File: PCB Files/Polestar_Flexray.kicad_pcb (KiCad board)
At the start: 4 copper layers, 82 x 43 mm, 80 parts, among them J1 JAE DX07S024XJ1R1100, J2 Molex 2125280400, J3 JAE MX34032NF4, J4 JAE MX34032NF4, K1 G5V-2-H1 DC12, K2 G5V-2-H1 DC12, K3 G5V-2-H1 DC12, Q1 DMN3200U-7, Q2 DMN3200U-7, Q3 DMP4015SSS-13, U1 Vishay DG419LEDY-T1-GE4, U2 Vishay DG419LEDY-T1-GE4, U3 LM53600LQDSXRQ1, U4 XIAO_RP2350, U5 TJA1082, U6 TJA1082, U8 TCAN4550-Q1, Y1 40MHz NX2016SA

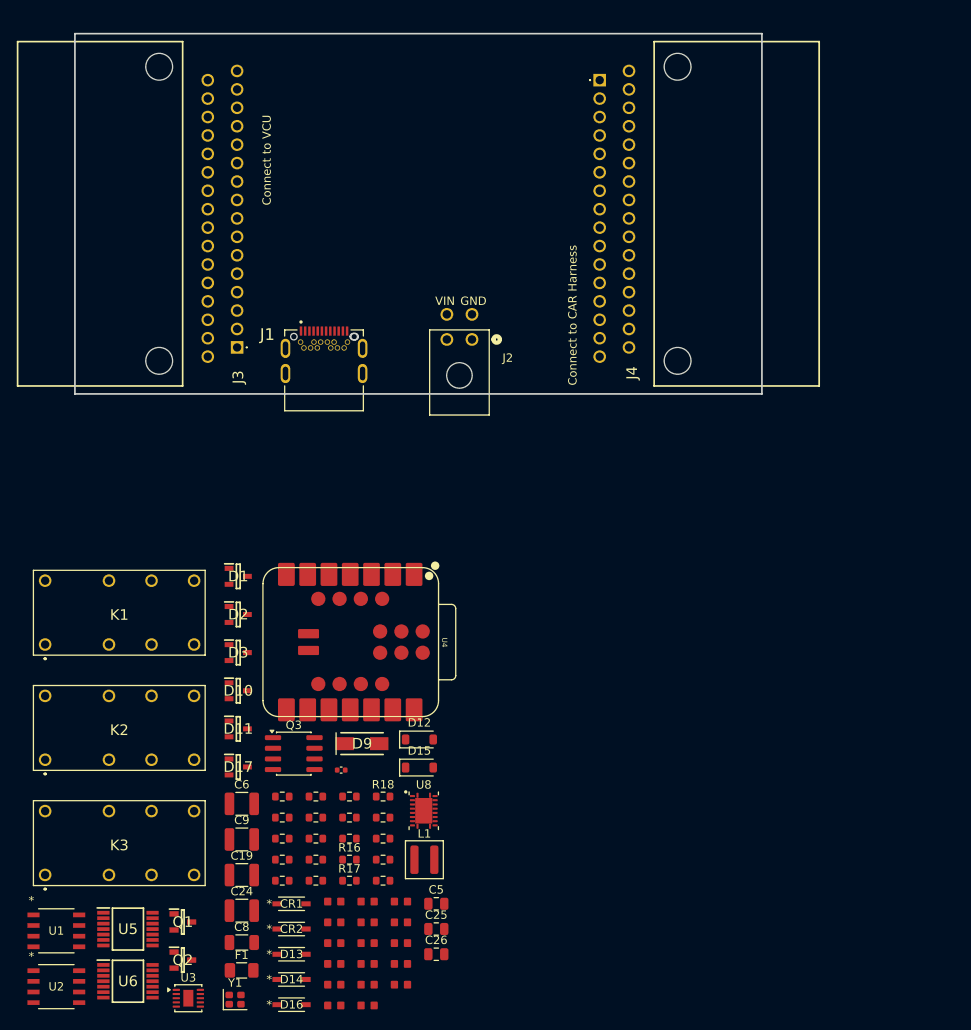
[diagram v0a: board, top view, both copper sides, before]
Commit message: Re-place board on 98x58 mm outline, add mounting holes and rounded corners
Placement
- Re-placed all 80 footprints to the "wide_2" layout on a 98 x 58 mm
  outline (was 119 x 43 mm). The 5 V buck block (U3, L1, C8-C12, C27,
  R13) and D9/C6 move to the bottom right, the SW_VCC group (D15, R21,
  D16) to the top left, and the comma CAN group (U1, U2, R2, R3, C28)
  shifts left. C11, D9, R13 and R21 also change rotation.
- Pad geometry, sizes, layers and nets verified unchanged across the
  rotations: 389 pads, 126 nets, 0 net changes.

Mechanical
- Added H1-H4: M3, 3.2 mm, non-plated, inset 3.8 mm from both edges.
  Non-plated so enclosure screws do not bond chassis to board ground;
  harness pin 13 is not board GND. PCB-only, no schematic symbols.
- Radiused the four board corners at R3.8 mm. Each arc centre lands on
  its mounting-hole centre, so the corner is concentric with the hole.
- Reshaped the In1.Cu ground pour outline to match the rounded corners
  and dropped its stale square-cornered fill so it repours correctly.

DRC
- Added Polestar_Flexray.kicad_dru. U8 reproduces TI drawing 4225320/A
  (RGY0020A) exactly, which places the exposed pad 0.025 mm from every
  perimeter pin; U3's 0.5 mm-pitch pins sit 0.26 mm apart against a
  0.3 mm Power netclass rule. Both are non-solder-mask-defined, so
  bridging is controlled by the stencil, not copper spacing. The rule
  is scoped to U3/U8 so other footprints are still checked normally.
- Raised U4's reference text from 0.635 mm to 1.0 mm to meet the
  0.8 mm board minimum.
- Now 0 clearance, 0 courtyard-overlap, 0 copper-to-edge and
  0 invalid-outline violations. Remaining items are the 239 unrouted
  ratsnest connections and cosmetic silkscreen warnings.

The board is still unrouted - 0 tracks, 0 vias. Do not fabricate.

Co-Authored-By: Claude Opus 5 <noreply@anthropic.com>
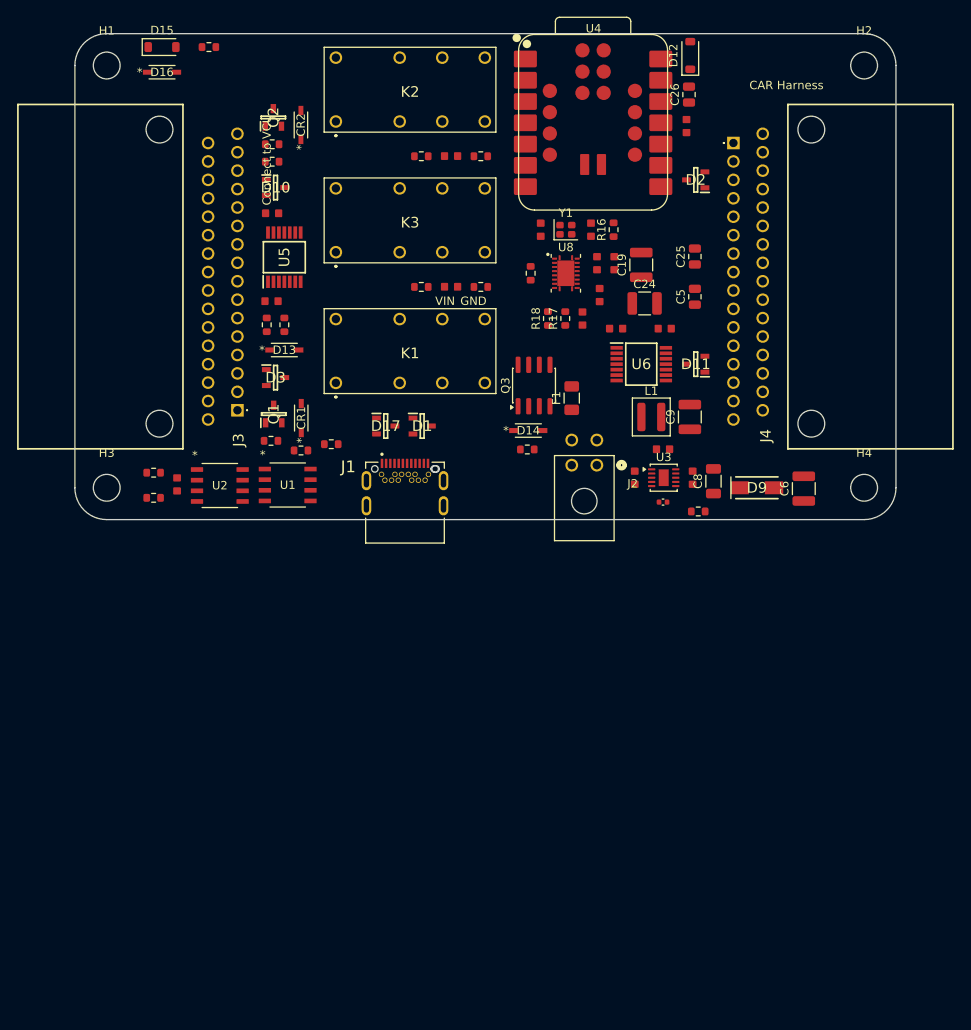
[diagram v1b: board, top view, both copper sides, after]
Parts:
- added H1: MountingHole_3.2mm_M3, MountingHole_3.2mm_M3, F.Cu at (105.8, 73.3)
- added H2: MountingHole_3.2mm_M3, MountingHole_3.2mm_M3, F.Cu at (196.2, 73.3)
- added H3: MountingHole_3.2mm_M3, MountingHole_3.2mm_M3, F.Cu at (105.8, 123.7)
- added H4: MountingHole_3.2mm_M3, MountingHole_3.2mm_M3, F.Cu at (196.2, 123.7)
- moved D16 112.4 mm to (112.4, 74.1)
- moved C7 110.8 mm to (175.0, 80.5), turned to 90 degrees
- moved C26 106.9 mm to (175.3, 76.8), turned to 90 degrees
- moved Q2 101.2 mm to (125.7, 79.5), turned to 90 degrees
- moved Y1 100.0 mm to (160.6, 92.9)
- moved R21 99.2 mm to (118.0, 71.1)
- moved C18 96.4 mm to (163.6, 92.9), turned to 90 degrees
- moved CR2 96.0 mm to (129.0, 80.4), turned to 90 degrees
- moved U6 95.8 mm to (169.6, 109.0)
- moved C13 94.5 mm to (146.9, 84.1)
- moved C17 92.4 mm to (157.6, 92.9), turned to 90 degrees
- moved D15 91.3 mm to (112.4, 71.1)
- moved D12 87.8 mm to (175.4, 72.1), turned to 90 degrees
- moved R12 87.4 mm to (143.3, 84.1)
- moved C19 87.0 mm to (169.6, 97.1), turned to 90 degrees
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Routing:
- added copper zone on In1.Cu, net GND
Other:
- board size 82 x 43 mm -> 98 x 58 mm
- board text added: "CAR Harness"
- board text removed: "Connect to CAR Harness"
